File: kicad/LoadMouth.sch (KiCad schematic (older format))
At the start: 15 parts, among them P1 CONN_01X02, P2 CONN_01X02, P3 CONN_01X02, Q1 Q_NPN_EBC

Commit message: Finalised the layout and created the Gerbers
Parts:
- added TP1, TP2: CONN_01X01, Pin_Headers:Pin_Header_Straight_1x01, symbol CONN_01X01
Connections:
- net Input: now also TP1.1 (P1)
- net Out: now also TP2.1 (P1)
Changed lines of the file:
@@
 Text Label 5000 3800 0    60   ~ 0
 Emitter
+$Comp
+L CONN_01X01 TP2
+U 1 1 55FC3DC4
+P 6150 2100
+F 0 "TP2" H 6150 2200 50  0000 C CNN
+F 1 "CONN_01X01" V 6250 2100 50  0000 C CNN
+F 2 "Pin_Headers:Pin_Header_Straight_1x01" H 6150 2100 60  0001 C CNN
+F 3 "" H 6150 2100 60  0000 C CNN
+	1    6150 2100
+	0    -1   -1   0
+$EndComp
+Wire Wire Line
+	6150 2400 6150 2300
+Connection ~ 6150 2400
+$Comp
+L CONN_01X01 TP1
+U 1 1 55FC3FCE
+P 2950 3150
+F 0 "TP1" H 2950 3250 50  0000 C CNN
+F 1 "CONN_01X01" V 3050 3150 50  0000 C CNN
+F 2 "Pin_Headers:Pin_Header_Straight_1x01" H 2950 3150 60  0001 C CNN
+F 3 "" H 2950 3150 60  0000 C CNN
+	1    2950 3150
+	0    -1   -1   0
+$EndComp
+Wire Wire Line
+	2950 3350 2950 3500
+Connection ~ 2950 3500
 $EndSCHEMATC

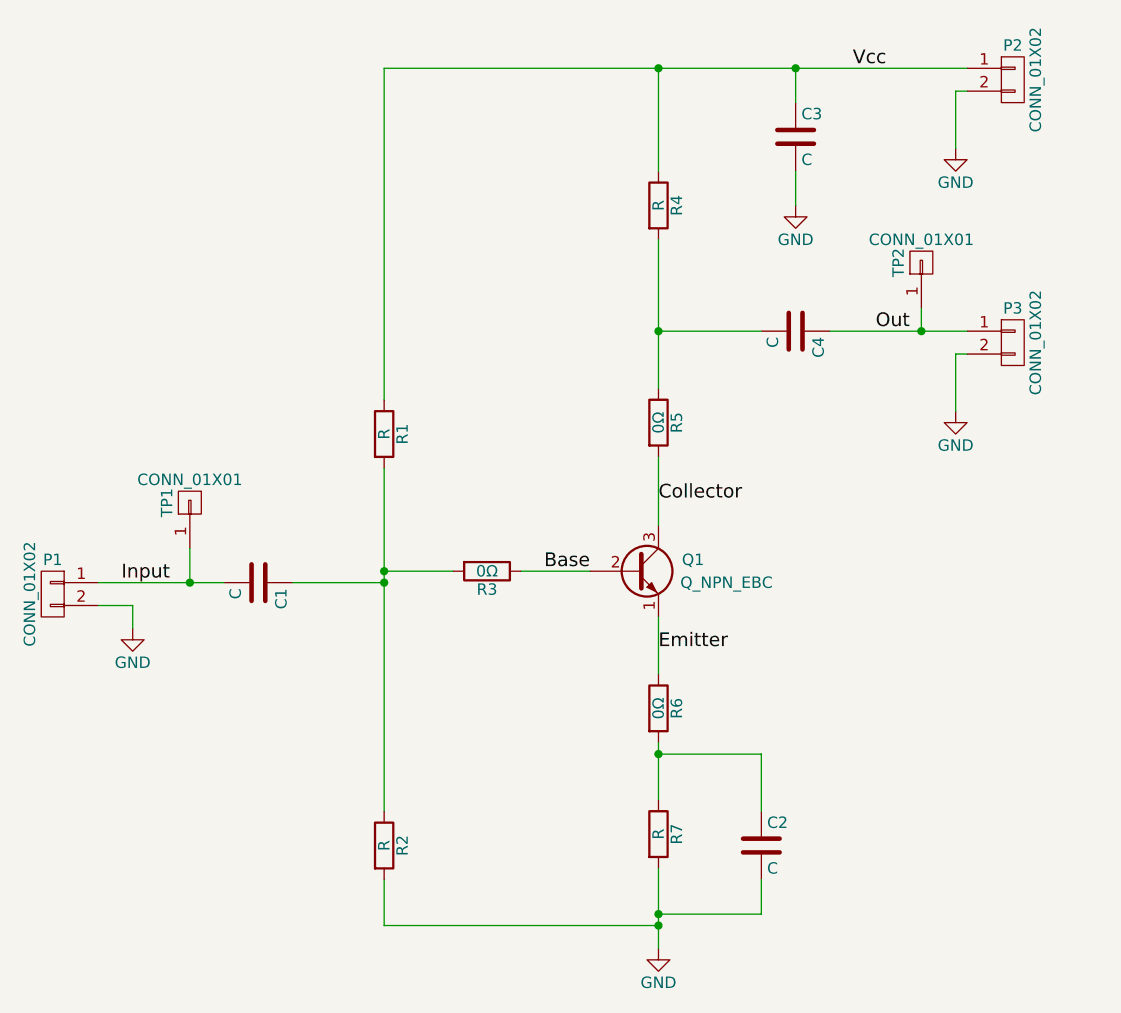
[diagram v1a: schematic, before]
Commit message: Added values for parts
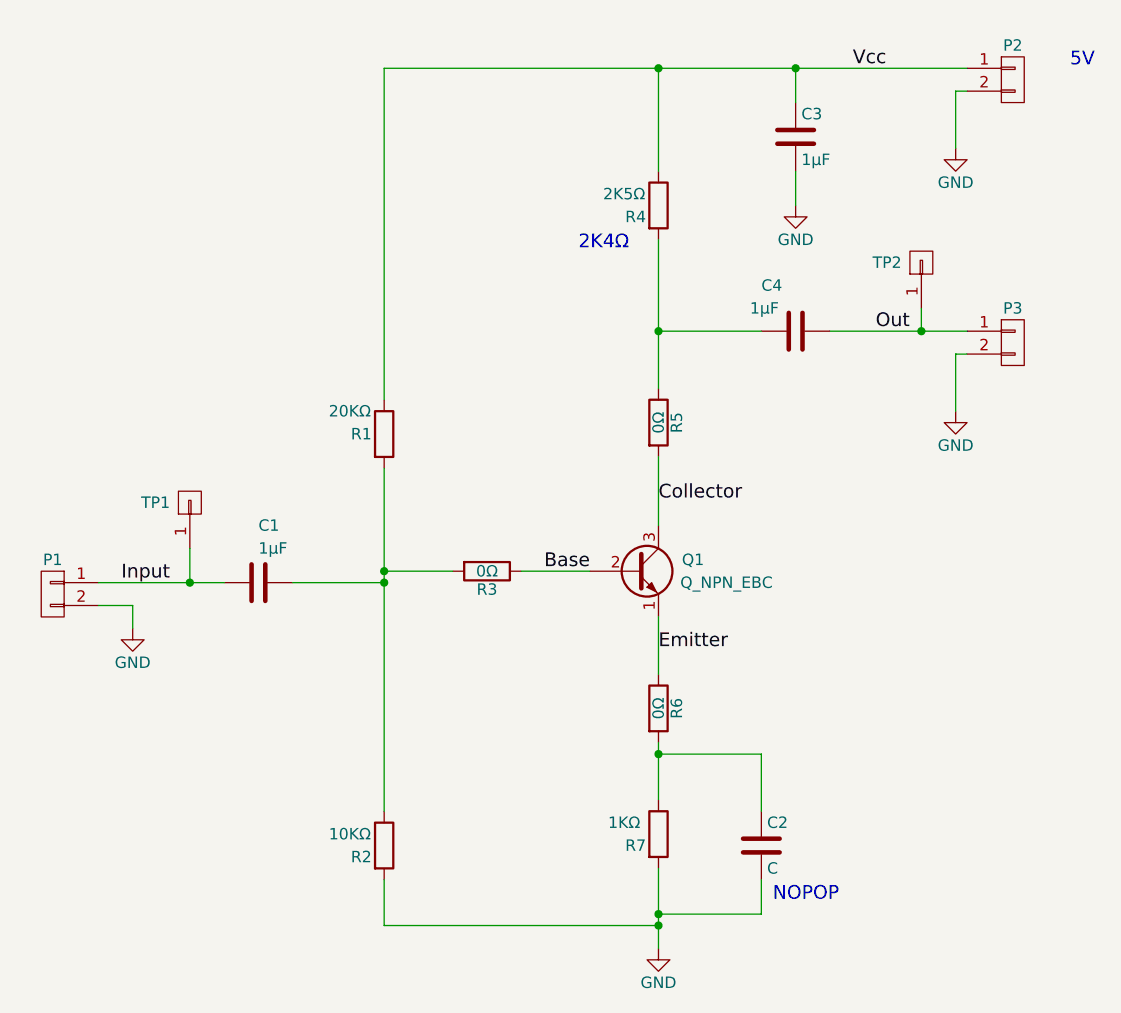
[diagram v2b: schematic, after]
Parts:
- C1, C3, C4: value C -> 1μF
- R1: value R -> 20KΩ
- R2: value R -> 10KΩ
- R4: value R -> 2K5Ω
- R7: value R -> 1KΩ
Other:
- note added: "2K4Ω"
- note added: "5V"
- note added: "NOPOP\n"
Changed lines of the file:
@@
 U 1 1 55FB0C0F
 P 5000 4600
-F 0 "R7" V 5080 4600 50  0000 C CNN
-F 1 "R" V 5000 4600 50  0000 C CNN
+F 0 "R7" H 4900 4550 50  0000 C CNN
+F 1 "1KΩ" H 4850 4650 50  0000 C CNN
 F 2 "Resistors_SMD:R_0805_HandSoldering" V 4930 4600 30  0001 C CNN
 F 3 "" H 5000 4600 30  0000 C CNN
@@
 U 1 1 55FB0C60
 P 5000 1850
-F 0 "R4" V 5080 1850 50  0000 C CNN
-F 1 "R" V 5000 1850 50  0000 C CNN
+F 0 "R4" H 4900 1800 50  0000 C CNN
+F 1 "2K5Ω" H 4850 1900 50  0000 C CNN
 F 2 "Resistors_SMD:R_0805_HandSoldering" V 4930 1850 30  0001 C CNN
 F 3 "" H 5000 1850 30  0000 C CNN
@@
 U 1 1 55FB0CED
 P 3800 2850
-F 0 "R1" V 3880 2850 50  0000 C CNN
-F 1 "R" V 3800 2850 50  0000 C CNN
+F 0 "R1" H 3700 2850 50  0000 C CNN
+F 1 "20KΩ" H 3650 2950 50  0000 C CNN
 F 2 "Resistors_SMD:R_0805_HandSoldering" V 3730 2850 30  0001 C CNN
 F 3 "" H 3800 2850 30  0000 C CNN
@@
 U 1 1 55FB0D8E
 P 3800 4650
-F 0 "R2" V 3880 4650 50  0000 C CNN
-F 1 "R" V 3800 4650 50  0000 C CNN
+F 0 "R2" H 3700 4600 50  0000 C CNN
+F 1 "10KΩ" H 3650 4700 50  0000 C CNN
 F 2 "Resistors_SMD:R_0805_HandSoldering" V 3730 4650 30  0001 C CNN
 F 3 "" H 3800 4650 30  0000 C CNN
@@
 P 5600 1550
 F 0 "C3" H 5625 1650 50  0000 L CNN
-F 1 "C" H 5625 1450 50  0000 L CNN
+F 1 "1μF" H 5625 1450 50  0000 L CNN
 F 2 "Capacitors_SMD:C_1210_HandSoldering" H 5638 1400 30  0001 C CNN
 F 3 "" H 5600 1550 60  0000 C CNN
@@
 U 1 1 55FB0E8E
 P 5600 2400
-F 0 "C4" H 5625 2500 50  0000 L CNN
-F 1 "C" H 5625 2300 50  0000 L CNN
+F 0 "C4" V 5400 2250 50  0000 L CNN
+F 1 "1μF" V 5500 2200 50  0000 L CNN
 F 2 "Capacitors_SMD:C_1210_HandSoldering" H 5638 2250 30  0001 C CNN
 F 3 "" H 5600 2400 60  0000 C CNN
@@
 U 1 1 55FB0EC7
 P 3250 3500
-F 0 "C1" H 3275 3600 50  0000 L CNN
-F 1 "C" H 3275 3400 50  0000 L CNN
+F 0 "C1" V 3000 3500 50  0000 L CNN
+F 1 "1μF" V 3100 3500 50  0000 L CNN
 F 2 "Capacitors_SMD:C_1210_HandSoldering" H 3288 3350 30  0001 C CNN
 F 3 "" H 3250 3500 60  0000 C CNN
@@
 P 6550 1300
 F 0 "P2" H 6550 1450 50  0000 C CNN
-F 1 "CONN_01X02" V 6650 1300 50  0000 C CNN
+F 1 "CONN_01X02" V 6650 1300 50  0001 C CNN
 F 2 "Pin_Headers:Pin_Header_Straight_1x02" H 6550 1300 60  0001 C CNN
 F 3 "" H 6550 1300 60  0000 C CNN
@@
 P 6550 2450
 F 0 "P3" H 6550 2600 50  0000 C CNN
-F 1 "CONN_01X02" V 6650 2450 50  0000 C CNN
+F 1 "CONN_01X02" V 6650 2450 50  0001 C CNN
 F 2 "Pin_Headers:Pin_Header_Straight_1x02" H 6550 2450 60  0001 C CNN
 F 3 "" H 6550 2450 60  0000 C CNN
@@
 P 2350 3550
 F 0 "P1" H 2350 3700 50  0000 C CNN
-F 1 "CONN_01X02" V 2450 3550 50  0000 C CNN
+F 1 "CONN_01X02" V 2450 3550 50  0001 C CNN
 F 2 "Pin_Headers:Pin_Header_Straight_1x02" H 2350 3550 60  0001 C CNN
 F 3 "" H 2350 3550 60  0000 C CNN
@@
 U 1 1 55FC3DC4
 P 6150 2100
-F 0 "TP2" H 6150 2200 50  0000 C CNN
-F 1 "CONN_01X01" V 6250 2100 50  0000 C CNN
+F 0 "TP2" V 6150 2250 50  0000 C CNN
+F 1 "CONN_01X01" V 6250 2100 50  0001 C CNN
 F 2 "Pin_Headers:Pin_Header_Straight_1x01" H 6150 2100 60  0001 C CNN
 F 3 "" H 6150 2100 60  0000 C CNN
@@
 U 1 1 55FC3FCE
 P 2950 3150
-F 0 "TP1" H 2950 3250 50  0000 C CNN
-F 1 "CONN_01X01" V 3050 3150 50  0000 C CNN
+F 0 "TP1" V 2950 3300 50  0000 C CNN
+F 1 "CONN_01X01" V 3050 3150 50  0001 C CNN
 F 2 "Pin_Headers:Pin_Header_Straight_1x01" H 2950 3150 60  0001 C CNN
 F 3 "" H 2950 3150 60  0000 C CNN
@@
 	2950 3350 2950 3500
 Connection ~ 2950 3500
+Text Notes 6800 1250 0    60   ~ 0
+5V
+Text Notes 5500 4900 0    60   ~ 0
+NOPOP\n
+Text Notes 4650 2050 0    60   ~ 0
+2K4Ω
 $EndSCHEMATC
